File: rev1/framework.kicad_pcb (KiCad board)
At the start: 2 copper layers, 238.1 x 375.5 mm, 190 parts, among them J1 AVR-ISP-6, J2 USB_C_Receptacle_USB2.0, SW1 SW_Push, SW10 SW_Push_45deg, SW11 SW_Push_45deg, SW12 SW_Push_45deg, SW13 SW_Push_45deg, SW14 SW_Push_45deg, SW15 SW_Push_45deg, SW16 SW_Push_45deg, SW17 SW_Push_45deg, SW18 SW_Push_45deg, SW19 SW_Push_45deg, SW2 SW_Push, SW20 SW_Push_45deg, SW21 SW_Push_45deg, SW22 SW_Push_45deg, SW23 SW_Push_45deg, SW24 SW_Push_45deg, SW25 SW_Push_45deg, SW26 SW_Push_45deg, SW27 SW_Push_45deg, SW28 SW_Push_45deg, SW29 SW_Push_45deg, SW3 SW_Push_45deg, SW30 SW_Push_45deg, SW31 SW_Push_45deg, SW32 SW_Push_45deg, SW33 SW_Push_45deg, SW34 SW_Push_45deg, SW35 SW_Push_45deg, SW36 SW_Push_45deg, SW37 SW_Push_45deg, SW38 SW_Push_45deg, SW39 SW_Push_45deg, SW4 SW_Push_45deg, SW40 SW_Push_45deg, SW41 SW_Push_45deg, SW42 SW_Push_45deg, SW43 SW_Push_45deg, SW44 SW_Push_45deg, SW45 SW_Push_45deg, SW46 SW_Push_45deg, SW47 SW_Push_45deg, SW48 SW_Push_45deg, SW49 SW_Push_45deg, SW5 SW_Push_45deg, SW50 SW_Push_45deg, SW51 SW_Push_45deg, SW52 SW_Push_45deg, SW53 SW_Push_45deg, SW54 SW_Push_45deg, SW55 SW_Push_45deg, SW56 SW_Push_45deg, SW57 SW_Push_45deg, SW58 SW_Push_45deg, SW59 SW_Push_45deg, SW6 SW_Push_45deg, SW60 SW_Push_45deg, SW61 SW_Push_45deg, SW62 SW_Push_45deg, SW63 Rotary_Encoder_Switch, SW64 SW_Push_45deg, SW65 SW_Push_45deg, SW7 SW_Push_45deg, SW8 SW_Push_45deg, SW9 SW_Push_45deg, U1 ATmega328P-PU, Y1 16M

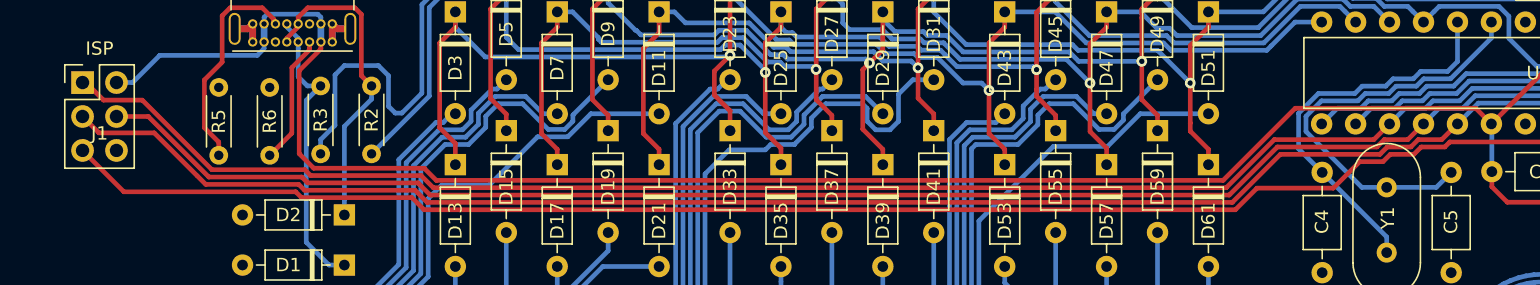
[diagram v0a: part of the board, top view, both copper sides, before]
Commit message: Fix mixed up MOSI and MISO connections for ISP
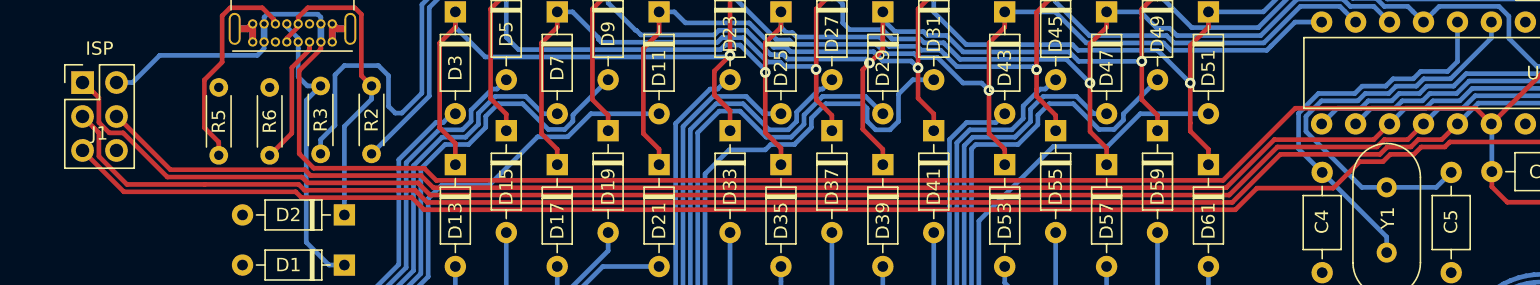
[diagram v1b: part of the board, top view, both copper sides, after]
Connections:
- J1 pad 1: mosi -> miso
- J1 pad 4: miso -> mosi
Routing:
- net miso: track 254.5 -> 259.4 mm
- net mosi: track 241.7 -> 238.1 mm
- net r9: track 260.2 -> 261.2 mm

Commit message: add acrylic cover + update schematic pdf
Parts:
- added REF**: MountingHole_2.2mm_M2, MountingHole:MountingHole_2.2mm_M2, F.Cu at (333.0, 363.1)
- added REF**: MountingHole_2.2mm_M2, MountingHole:MountingHole_2.2mm_M2, F.Cu at (217.6, 361.9)
- added REF**: MountingHole_2.2mm_M2, MountingHole:MountingHole_2.2mm_M2, F.Cu at (102.1, 363.1)
- added REF**: MountingHole_2.2mm_M2, MountingHole:MountingHole_2.2mm_M2, F.Cu at (217.6, 226.6)
- added REF**: MountingHole_2.2mm_M2, MountingHole:MountingHole_2.2mm_M2, F.Cu at (333.0, 227.8)
- added REF**: MountingHole_2.2mm_M2, MountingHole:MountingHole_2.2mm_M2, F.Cu at (102.1, 227.8)
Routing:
- net +5V: track 166.3 -> 164.9 mm

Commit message: board aesthetic changes
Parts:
- removed the G*** at (217.4, 403.5)
- added G***: LOGO, framework:7c8small, B.Cu at (257.0, 328.9)
- added G***: LOGO, framework:7c8, B.Cu at (113.0, 456.4)
- moved G*** 7.11 mm to (285.1, 327.4)
- moved G*** 7.11 mm to (281.7, 332.0)

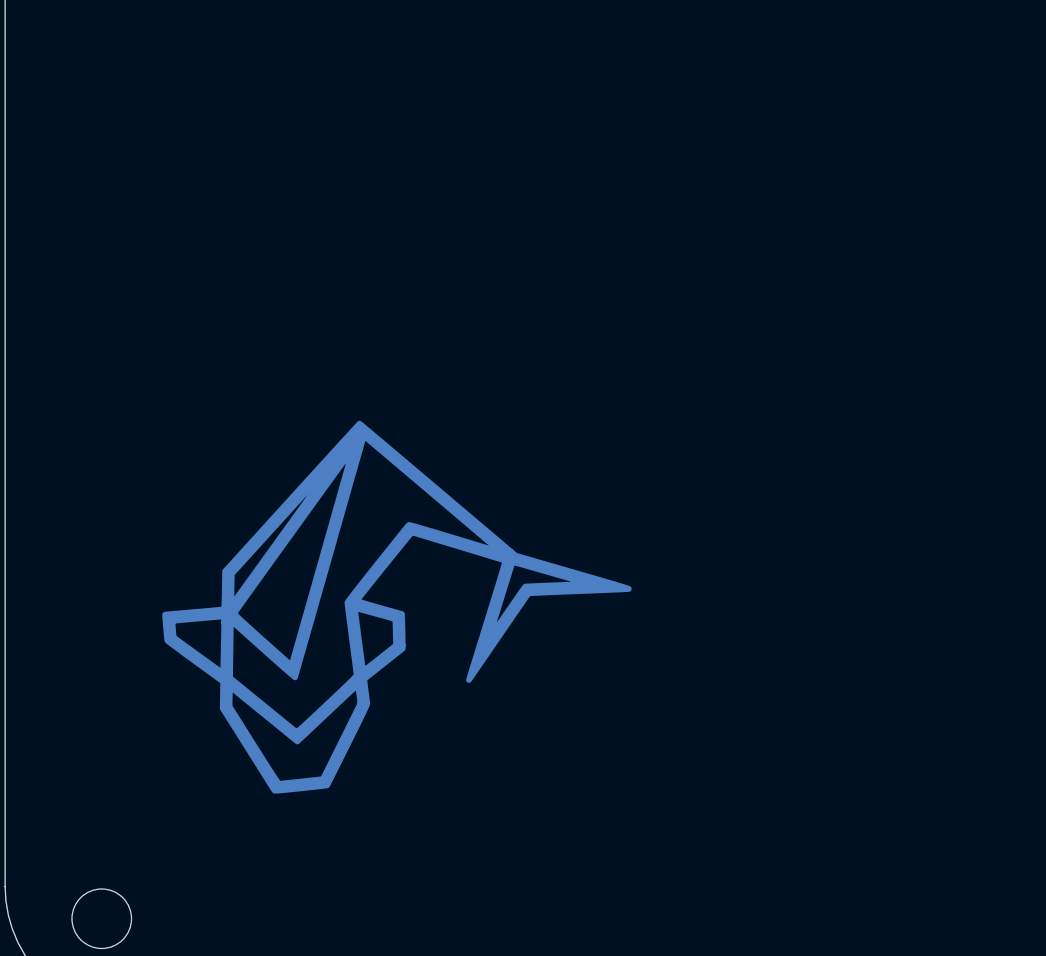
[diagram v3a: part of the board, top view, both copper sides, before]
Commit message: move fish logo slightly
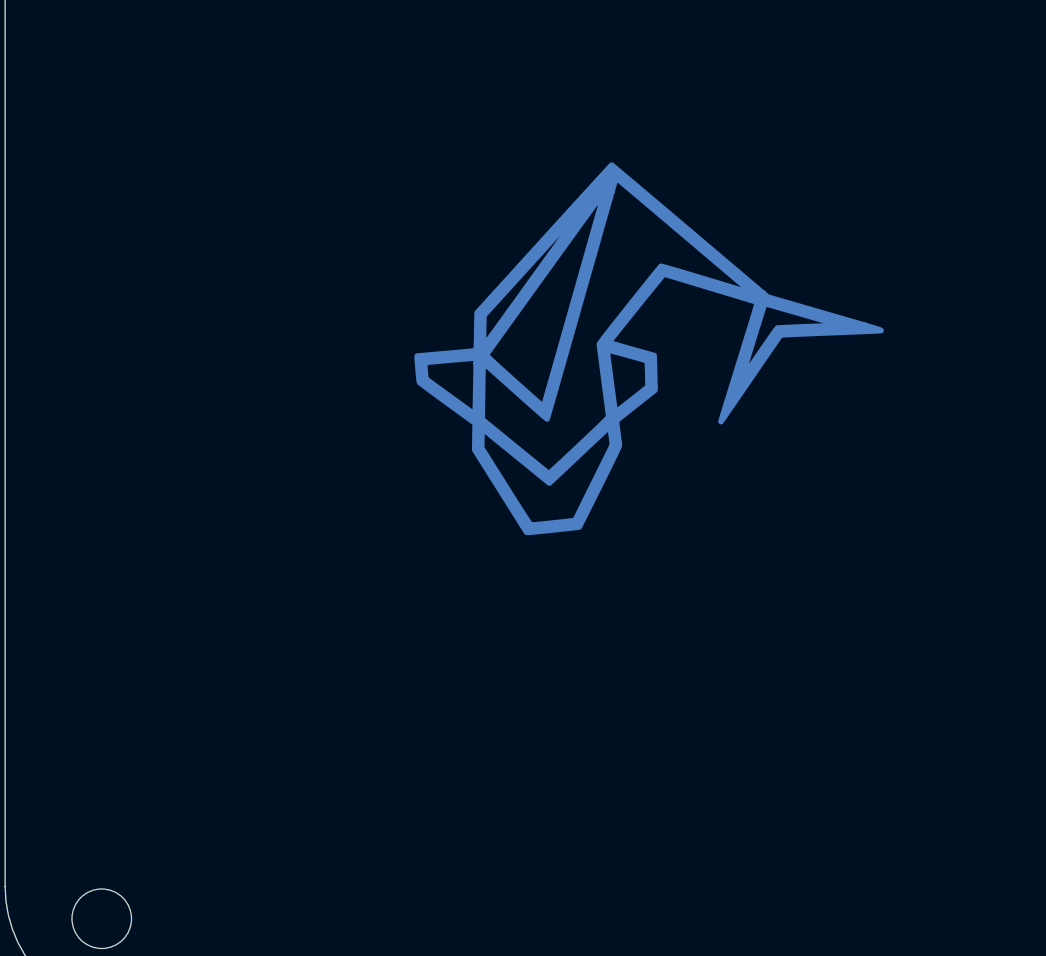
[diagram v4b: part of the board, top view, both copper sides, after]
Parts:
- moved G*** 13.3 mm to (122.3, 446.8)
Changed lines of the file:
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@@
   )
   (module framework:7c8 (layer B.Cu)
-    (at 112.982375 456.390375 180)
+    (at 122.301085 446.834515 180)
     (fp_text reference G*** (at 0 0) (layer B.SilkS) hide
       (effects (font (size 1.524 1.524) (thickness 0.3)) (justify mirror))

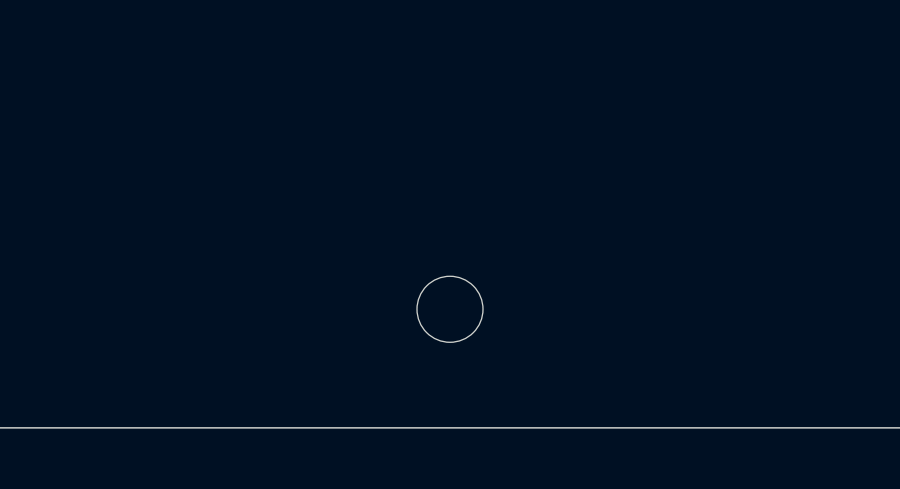
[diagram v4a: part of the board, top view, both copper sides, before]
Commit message: fix mounting hole misalignment on backplate
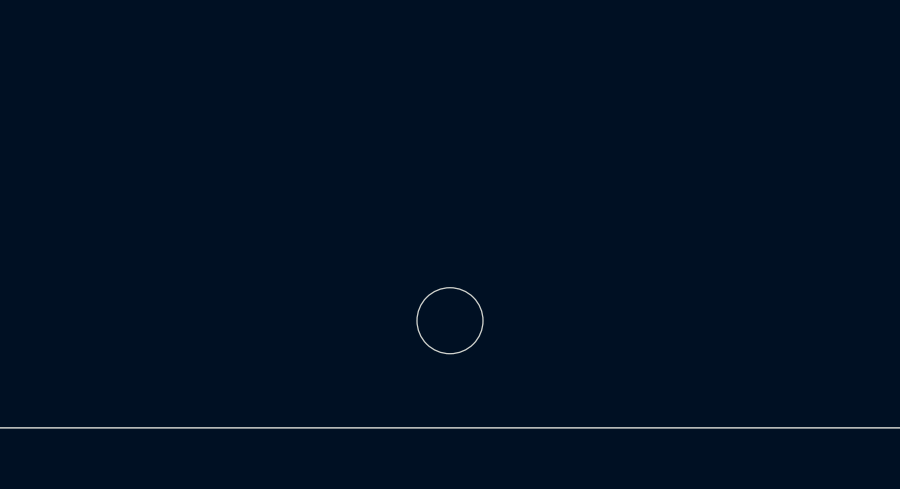
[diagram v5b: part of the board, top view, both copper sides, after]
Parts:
- moved REF** 0.38 mm to (217.6, 467.9)
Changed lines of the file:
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@@
     (solder_mask_min_width 0.25)
     (aux_axis_origin 0 0)
-    (grid_origin 217.551485 332.534035)
+    (grid_origin 102.060375 467.883625)
     (visible_elements 7FFFFF7F)
     (pcbplotparams
@@
   )
   (module MountingHole:MountingHole_2.2mm_M2 (layer F.Cu)
-    (at 217.551 467.502375)
+    (at 217.551 467.883625)
     (descr "Mounting Hole 2.2mm, no annular, M2")
     (tags "mounting hole 2.2mm no annular m2")
